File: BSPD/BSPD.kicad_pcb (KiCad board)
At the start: 2 copper layers, 81 x 61 mm, 37 parts, among them Q1 Q_NMOS_GSD, Q2 Q_NMOS_GSD, U101 641964-1, U102 641964-1, U103 R-78E5.0-0.5, U104 SN74LVC1G08DBVR, U105 LM339DR, U106 NE555DR, U107 SN74LVC3G14DCUR, U108 SN74AC32DR, U109 SN74LVC1G08DBVR, U110 641964-1, U111 641964-1

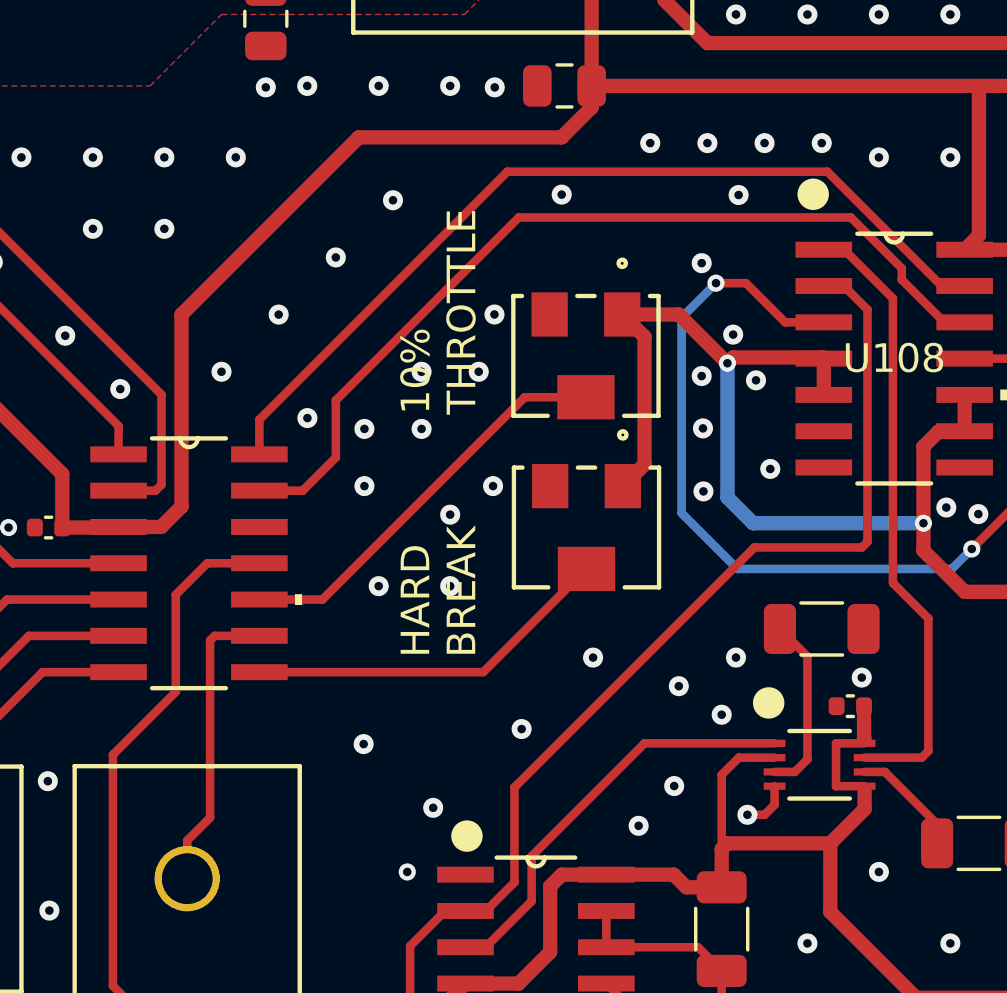
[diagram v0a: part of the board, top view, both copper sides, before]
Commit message: Double checked schematic. Fixed wrong connection on comparators and did re-routed the signals. Added new simulation with 555 timer and double cchecked that it is active low performing
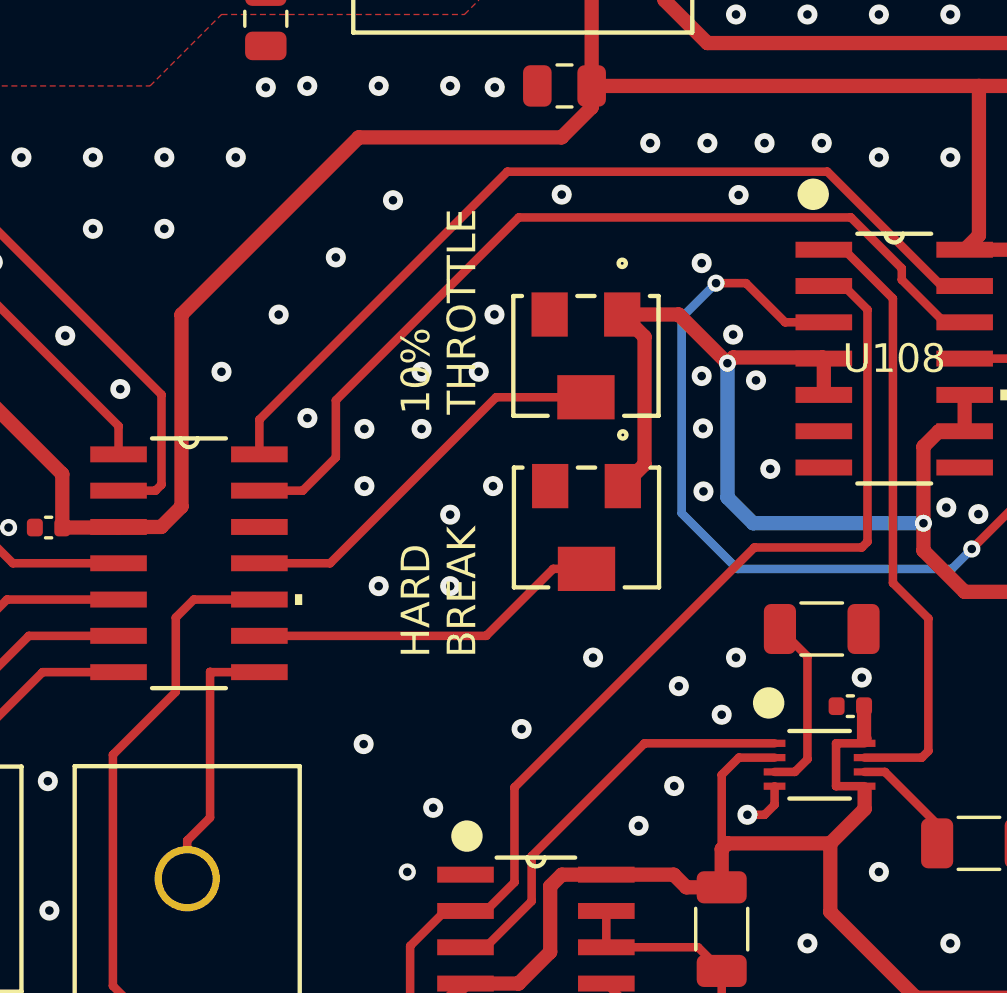
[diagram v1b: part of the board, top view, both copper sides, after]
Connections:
- U105 pad 10: 10%_THROTTLE -> THROTTLE_Sense_IN
- U105 pad 11: THROTTLE_Sense_IN -> 10%_THROTTLE
- U105 pad 8: HARD_BREAK -> BSE_Sense_IN
- U105 pad 9: BSE_Sense_IN -> HARD_BREAK
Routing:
- net BSE_Sense_IN: track 11.0 -> 9.86 mm
- net 10%_THROTTLE: track 14.4 -> 13.3 mm
- net THROTTLE_Sense_IN: track 21.7 -> 20.7 mm
- net HARD_BREAK: track 12.9 -> 12.4 mm
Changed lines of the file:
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@@
 			(at -2.7178 -5.5118 0)
 			(unlocked yes)
-			(layer "F.Fab")
+			(layer "F.SilkS")
 			(effects
 				(font
@@
 			)
 		)
-		(fp_text user "${REFERENCE}"
-			(at 0 0 0)
+		(fp_text user "*"
+			(at -2.7178 -5.5118 0)
+			(layer "F.SilkS")
+			(effects
+				(font
+					(size 1 1)
+					(thickness 0.15)
+				)
+			)
+		)
+		(fp_text user "*"
+			(at -2.7178 -5.5118 0)
 			(unlocked yes)
 			(layer "F.Fab")
@@
 			)
 		)
+		(fp_text user "${REFERENCE}"
+			(at 0 0 0)
+			(unlocked yes)
+			(layer "F.Fab")
+			(effects
+				(font
+					(size 1 1)
+					(thickness 0.15)
+				)
+			)
+		)
 		(pad "1" smd rect
 			(at -2.4638 -3.81)
@@
 			(size 1.9812 0.5588)
 			(layers "F.Cu" "F.Mask" "F.Paste")
-			(net 12 "HARD_BREAK")
+			(net 28 "BSE_Sense_IN")
 			(pinfunction "3IN-")
 			(pintype "input")
@@
 			(size 1.9812 0.5588)
 			(layers "F.Cu" "F.Mask" "F.Paste")
-			(net 28 "BSE_Sense_IN")
+			(net 12 "HARD_BREAK")
 			(pinfunction "3IN+")
 			(pintype "input")
@@
 			(size 1.9812 0.5588)
 			(layers "F.Cu" "F.Mask" "F.Paste")
-			(net 11 "10%_THROTTLE")
+			(net 27 "THROTTLE_Sense_IN")
 			(pinfunction "4IN-")
 			(pintype "input")
@@
 			(size 1.9812 0.5588)
 			(layers "F.Cu" "F.Mask" "F.Paste")
-			(net 27 "THROTTLE_Sense_IN")
+			(net 11 "10%_THROTTLE")
 			(pinfunction "4IN+")
 			(pintype "input")
@@
 	)
 	(segment
-		(start 152.0249 111.07)
-		(end 154.23 111.07)
+		(start 160.3077 103.9923)
+		(end 154.5 109.8)
 		(width 0.3)
 		(layer "F.Cu")
@@
 	)
 	(segment
-		(start 161.3077 103.9923)
-		(end 163.45 103.9923)
+		(start 163.45 103.9923)
+		(end 160.3077 103.9923)
 		(width 0.3)
 		(layer "F.Cu")
@@
 	)
 	(segment
-		(start 154.23 111.07)
-		(end 161.3077 103.9923)
+		(start 154.5 109.8)
+		(end 152.5259 109.8)
 		(width 0.3)
 		(layer "F.Cu")
@@
 	)
 	(segment
-		(start 152.0249 113.61)
-		(end 159.8556 113.61)
+		(start 162.3044 109.9956)
+		(end 159.96 112.34)
+		(width 0.3)
+		(layer "F.Cu")
+		(net 12)
+	)
+	(segment
+		(start 163.47 109.9956)
+		(end 162.3044 109.9956)
 		(width 0.3)
 		(layer "F.Cu")
@@
 	)
 	(segment
-		(start 159.8556 113.61)
-		(end 163.47 109.9956)
+		(start 159.96 112.34)
+		(end 152.0249 112.34)
 		(width 0.3)
 		(layer "F.Cu")
@@
 	)
 	(segment
-		(start 149.1 114.3)
-		(end 149.1 110.9)
+		(start 146.9 116.5)
+		(end 149.1 114.3)
 		(width 0.3)
 		(layer "F.Cu")
@@
 	)
 	(segment
-		(start 149.1 110.9)
-		(end 150.2 109.8)
+		(start 146.9 124.586)
+		(end 146.9 116.5)
 		(width 0.3)
 		(layer "F.Cu")
@@
 	)
 	(segment
-		(start 146.9 116.5)
-		(end 149.1 114.3)
+		(start 149.1 114.3)
+		(end 149.1 111.7)
 		(width 0.3)
 		(layer "F.Cu")
@@
 	)
 	(segment
-		(start 146.9 124.586)
-		(end 146.9 116.5)
+		(start 149.1 111.7)
+		(end 149.73 111.07)
 		(width 0.3)
 		(layer "F.Cu")
@@
 	)
 	(segment
-		(start 150.2 109.8)
-		(end 152.0249 109.8)
+		(start 149.73 111.07)
+		(end 152.0249 111.07)
 		(width 0.3)
 		(layer "F.Cu")
@@
 	)
 	(segment
-		(start 150.3 118.7)
-		(end 149.5 119.5)
+		(start 149.5 119.5)
+		(end 149.5 120.836)
 		(width 0.3)
 		(layer "F.Cu")
@@
 	)
 	(segment
-		(start 149.5 119.5)
-		(end 149.5 120.836)
+		(start 149.5 120.836)
+		(end 149.9 120.436)
 		(width 0.3)
 		(layer "F.Cu")
@@
 	)
 	(segment
-		(start 149.5 120.836)
-		(end 149.9 120.436)
+		(start 150.3 118.7)
+		(end 149.5 119.5)
 		(width 0.3)
 		(layer "F.Cu")
@@
 	)
 	(segment
-		(start 150.3 112.5)
+		(start 150.3 113.6)
 		(end 150.3 118.7)
 		(width 0.3)
@@
 	)
 	(segment
-		(start 150.46 112.34)
-		(end 150.3 112.5)
+		(start 150.31 113.61)
+		(end 152.0249 113.61)
 		(width 0.3)
 		(layer "F.Cu")
@@
 	)
 	(segment
-		(start 152.0249 112.34)
-		(end 150.46 112.34)
+		(start 150.3 113.6)
+		(end 150.31 113.61)
 		(width 0.3)
 		(layer "F.Cu")
